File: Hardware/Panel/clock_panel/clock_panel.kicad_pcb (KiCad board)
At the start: 2 copper layers, 50 x 200 mm, 18 parts

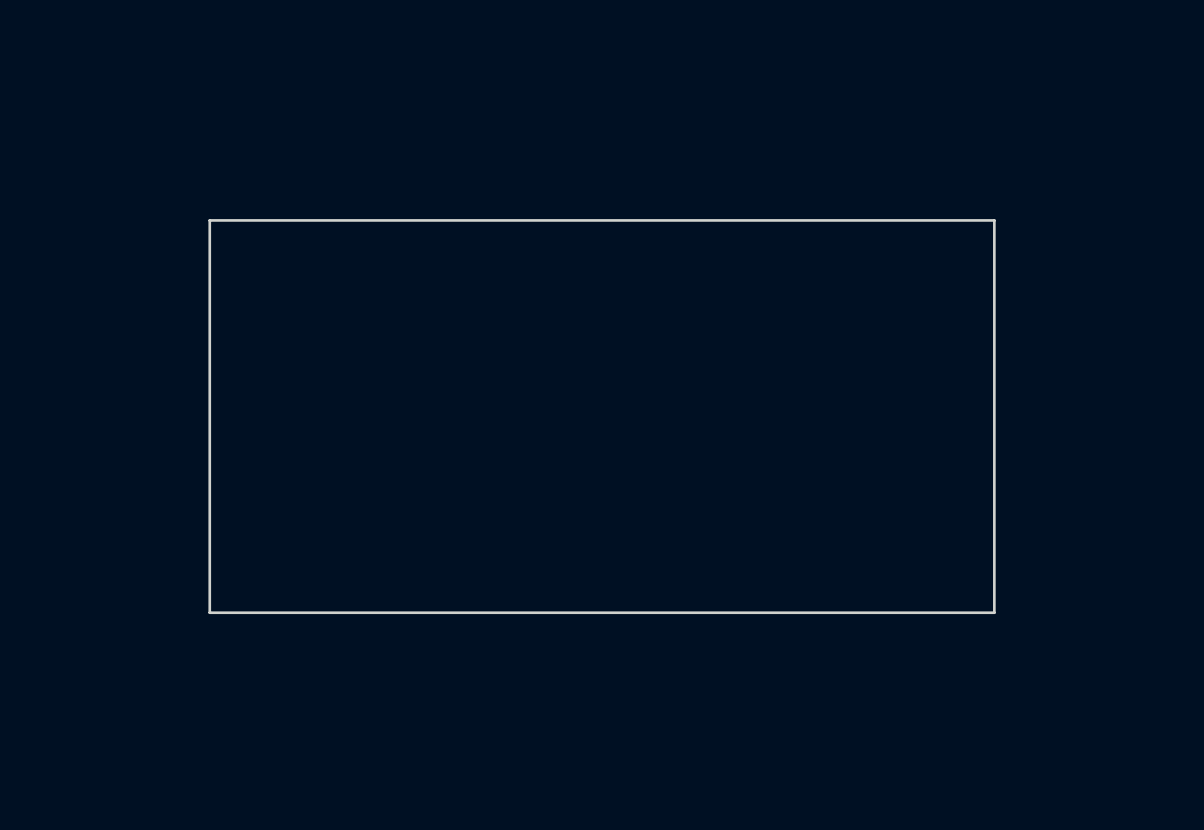
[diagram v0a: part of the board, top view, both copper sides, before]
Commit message: typo; OLED panel footprint
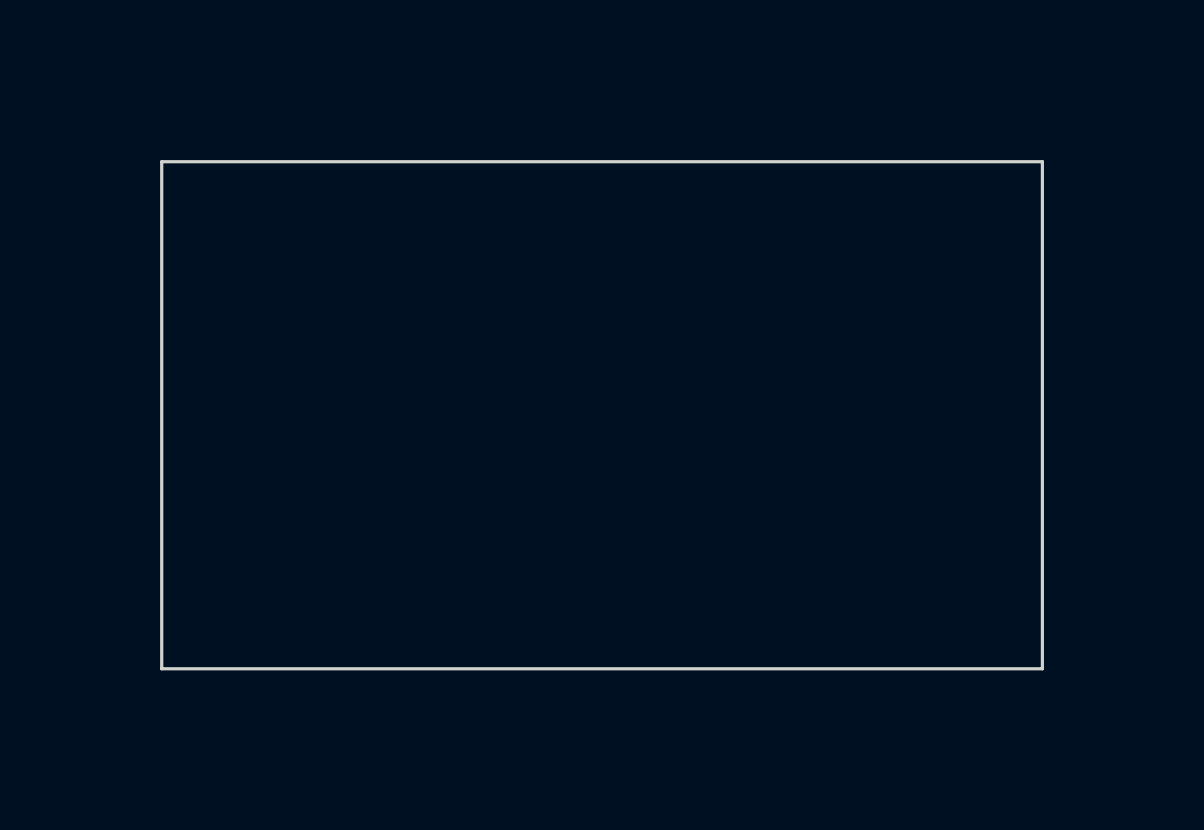
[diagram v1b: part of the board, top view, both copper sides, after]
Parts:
- added OLED1: OLED_128X64_Hole, Kosmo_panel:OLED_128x64_1.3in, F.Cu at (41.1, 37.5)
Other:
- outline, holes or cut-outs redrawn
